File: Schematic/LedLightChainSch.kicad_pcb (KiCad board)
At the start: 2 copper layers, 35.6 x 17.8 mm, 13 parts, among them J1 Led-Chain, J2 Out+, J3 Out-, J4 Batt+, J5 Batt-, J6 SWDIO, J7 TX, J8 Battery, Q1 BC817, SW1 SW_SPDT, U1 CH32V003JxMx

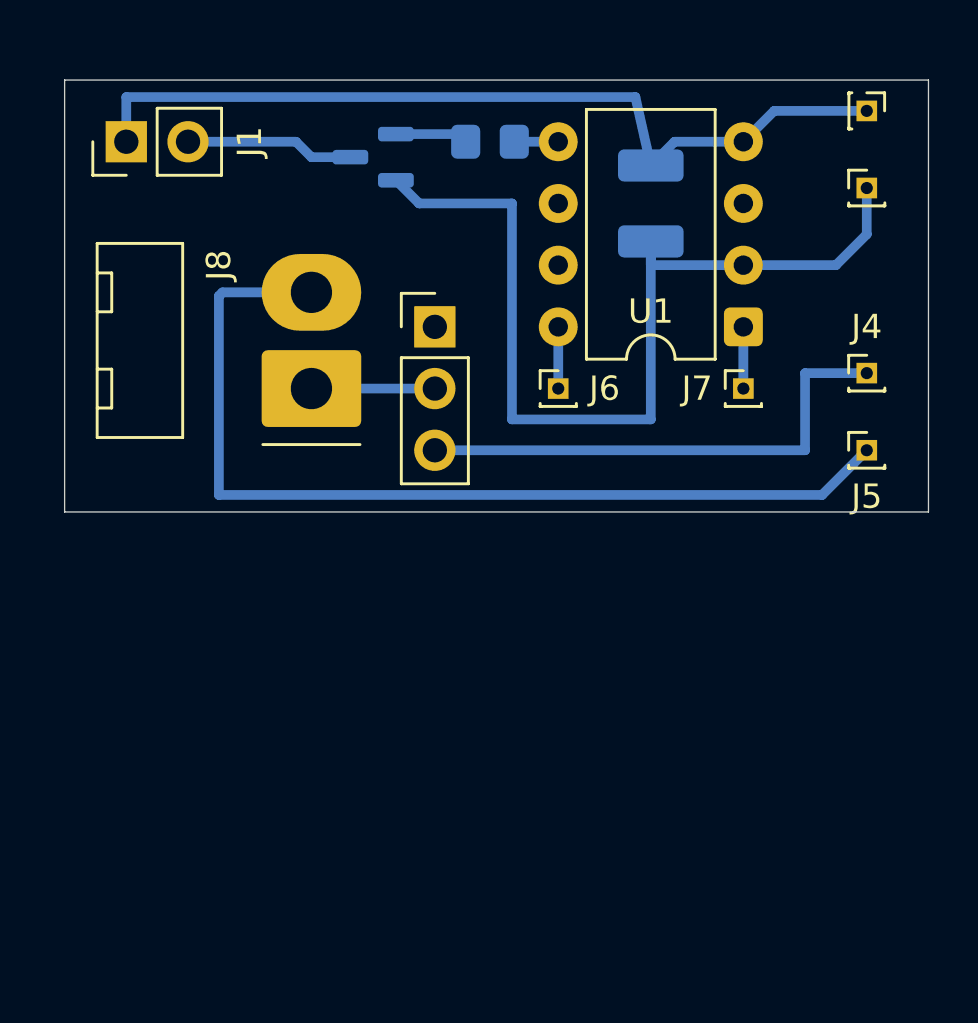
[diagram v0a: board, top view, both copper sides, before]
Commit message: PCB Battery-Board connections fixed.
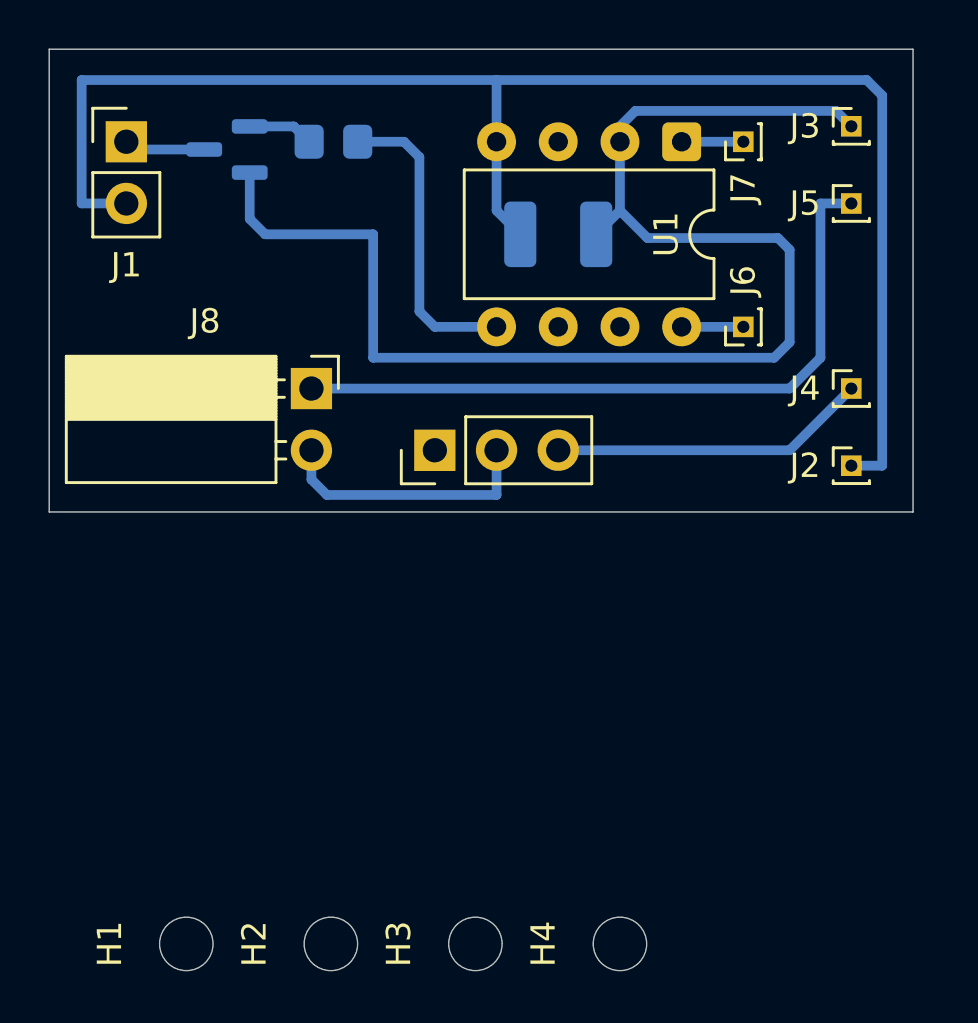
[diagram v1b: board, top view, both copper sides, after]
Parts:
- added H1: MountingHole, MountingHole:MountingHole_2.2mm_M2, F.Cu at (119.3, 127.0)
- added H2: MountingHole, MountingHole:MountingHole_2.2mm_M2, F.Cu at (125.3, 127.0)
- added H3: MountingHole, MountingHole:MountingHole_2.2mm_M2, F.Cu at (131.2, 127.0)
- added H4: MountingHole, MountingHole:MountingHole_2.2mm_M2, F.Cu at (137.2, 127.0)
- J8: footprint Connector_Molex:Molex_KK-396_A-41792-0002_1x02_P3.96mm_Horizontal -> Connector_PinSocket_2.54mm:PinSocket_1x02_P2.54mm_Horizontal
- moved J2 14.6 mm to (146.7, 107.3), turned to 0 degrees
- moved J5 10.2 mm to (146.7, 96.5)
- moved J7 10.2 mm to (142.2, 94.0), turned to 90 degrees
- moved J6 8.03 mm to (142.2, 101.6), turned to 90 degrees
- moved U1 8.03 mm to (139.7, 94.0), turned to -90 degrees
- moved R1 6.45 mm to (125.4, 94.0)
- moved Q1 6.03 mm to (121.0, 94.3)
- moved SW1 5.08 mm to (129.5, 106.7), turned to 90 degrees
- moved C1 4.02 mm to (134.6, 97.8), turned to 0 degrees
- moved J3 2.62 mm to (146.7, 93.3)
- moved J4 0.90 mm to (146.7, 104.1)
- turned J1 to 0 degrees
- turned J8 to 0 degrees
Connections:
- J1 pad 1: +4V -> Net-(J1-Pin_1)
- J1 pad 2: Net-(J1-Pin_2) -> +4V
- J8 pad 1: Net-(J8-Pin_1) -> Net-(J5-Pin_1)
- J8 pad 2: Net-(J5-Pin_1) -> Net-(J8-Pin_2)
- Q1 pad 3: Net-(J1-Pin_2) -> Net-(J1-Pin_1)
- SW1 pad 2: Net-(J8-Pin_1) -> Net-(J8-Pin_2)
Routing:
- net +4V: track 35.5 -> 63.4 mm
- net GND: track 39.4 -> 56.1 mm
- net Net-(J8-Pin_2): track 0.00 -> 10.9 mm
- net Net-(U1-PC1): track 1.81 -> 12.6 mm
- net Net-(J5-Pin_1): track 39.5 -> 29.1 mm
- net Net-(J4-Pin_1): track 21.0 -> 13.1 mm
- net Net-(J1-Pin_2): track 6.95 -> 0.00 mm
- net Net-(J8-Pin_1): track 5.08 -> 0.00 mm
- net Net-(J1-Pin_1): track 0.00 -> 3.34 mm
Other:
- board size 35.6 x 17.8 mm -> 35.6 x 19 mm

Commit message: Transistor removed
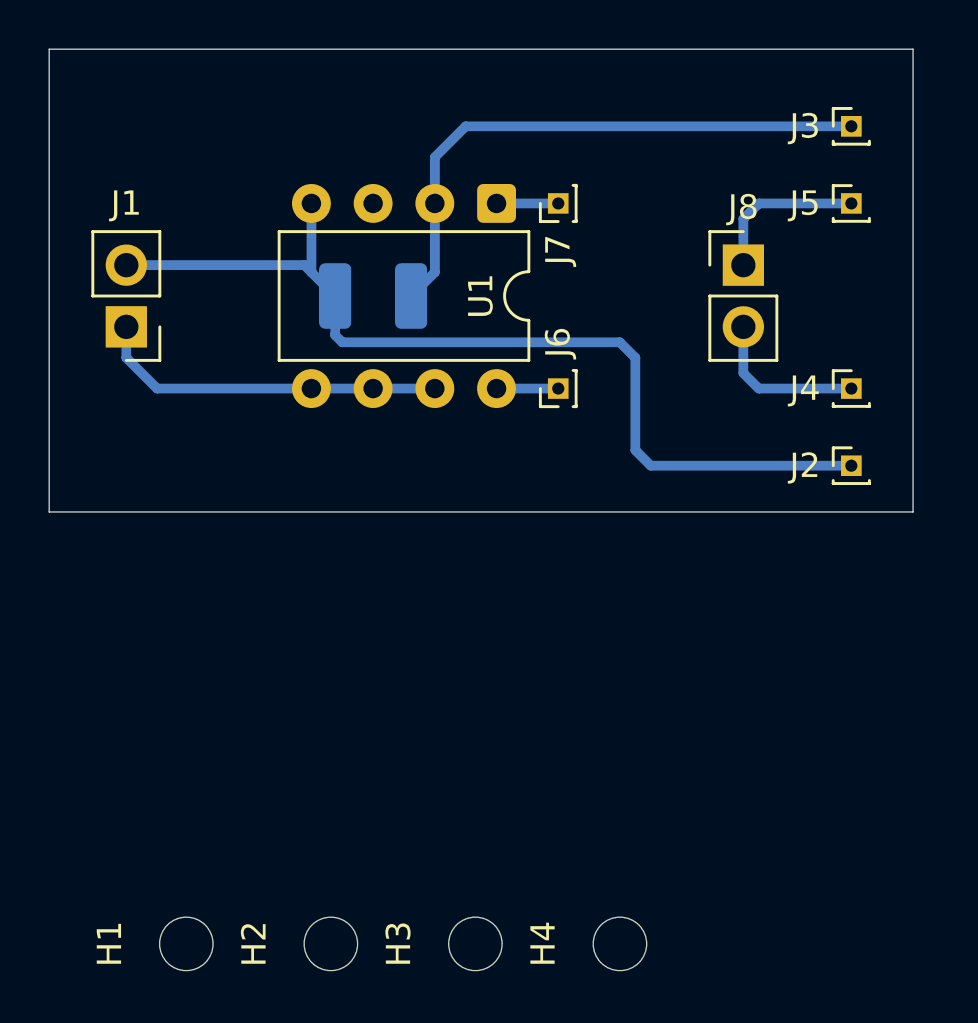
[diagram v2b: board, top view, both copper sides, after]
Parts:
- removed Q1: BC817, Package_TO_SOT_SMD:SOT-23
- removed R1: 4.7k, Resistor_SMD:R_0805_2012Metric_Pad1.20x1.40mm_HandSolder
- removed SW1: SW_SPDT, Connector_PinHeader_2.54mm:PinHeader_1x03_P2.54mm_Vertical
- J8: footprint Connector_PinSocket_2.54mm:PinSocket_1x02_P2.54mm_Horizontal -> Connector_PinHeader_2.54mm:PinHeader_1x02_P2.54mm_Vertical
- moved J8 18.5 mm to (142.2, 99.1)
- moved J6 8.03 mm to (134.6, 104.1)
- moved C1 8.03 mm to (127.0, 100.3)
- moved J7 8.03 mm to (134.6, 96.5)
- moved U1 8.03 mm to (132.1, 96.5)
- moved J1 7.62 mm to (116.8, 101.6), turned to 180 degrees
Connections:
- J8 pad 2: Net-(J8-Pin_2) -> Net-(J4-Pin_1)
- U1 pad 5: Net-(U1-PC1) -> Net-(J1-Pin_1)
- U1 pad 6: unconnected-(U1-PC2-Pad6) -> Net-(J1-Pin_1)
- U1 pad 7: unconnected-(U1-PC4-Pad7) -> Net-(J1-Pin_1)
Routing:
- net GND: track 56.1 -> 23.8 mm
- net +4V: track 63.4 -> 39.3 mm
- net Net-(J5-Pin_1): track 29.1 -> 6.61 mm
- net Net-(U1-PC1): track 12.6 -> 0.00 mm
- net Net-(J1-Pin_1): track 3.34 -> 14.5 mm
- net Net-(J8-Pin_2): track 10.9 -> 0.00 mm
- net Net-(J4-Pin_1): track 13.1 -> 6.61 mm
- net Net-(Q1-B): track 2.71 -> 0.00 mm
